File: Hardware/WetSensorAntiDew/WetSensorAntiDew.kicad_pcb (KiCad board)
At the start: 2 copper layers, 38.1 x 48.8 mm, 30 parts, among them J2 Connector to BME280, J3 4P4C, J5 Connector to power supply, J6 Conn_01x04_Socket, J8 6P6C, Q1 MOSFET N-CH, SW1 SW_Push, U1 AMS1117, U3 STM32F103C6Tx, Y1 Crystal_GND24_Small

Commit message: added USNA logo
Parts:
- added ?: LOGO, footprints:Anchors Aweigh, B.Cu at (112.1, 112.6)
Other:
- outline, holes or cut-outs redrawn

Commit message: shrunk anchors aweigh
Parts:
- moved ? 21.9 mm to (129.0, 98.7)

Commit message: USNA emblem tweaks
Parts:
- moved ? 23.1 mm to (107.2, 106.2)
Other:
- board text added: "Go Navy Beat Army"

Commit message: Added Semper Supra :)
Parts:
- added G***: LOGO, footprints:Semper Supra, B.Cu at (125.1, 109.3)

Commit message: Finalized silkscreen
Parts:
- added G***: LOGO, footprints:Evergreen, B.Cu at (98.1, 93.4)
- moved G*** 0.18 mm to (124.9, 109.3)
- renumbered SW1 to RESET
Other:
- board text added: "Go Navy, Beat Army"
- board text added: "V D C G"
- board text removed: "Go Navy Beat Army"

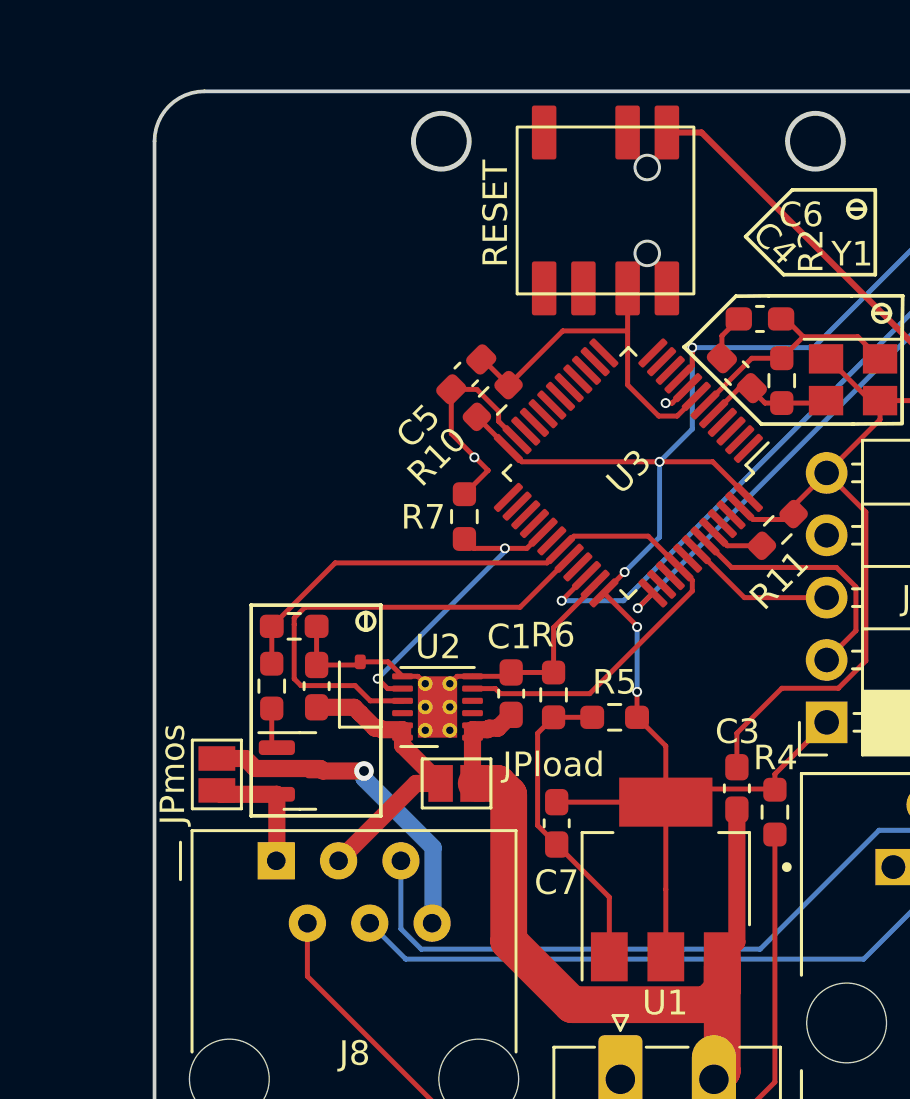
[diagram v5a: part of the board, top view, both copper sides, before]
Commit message: Tuned pinouts, corrected N/P switches
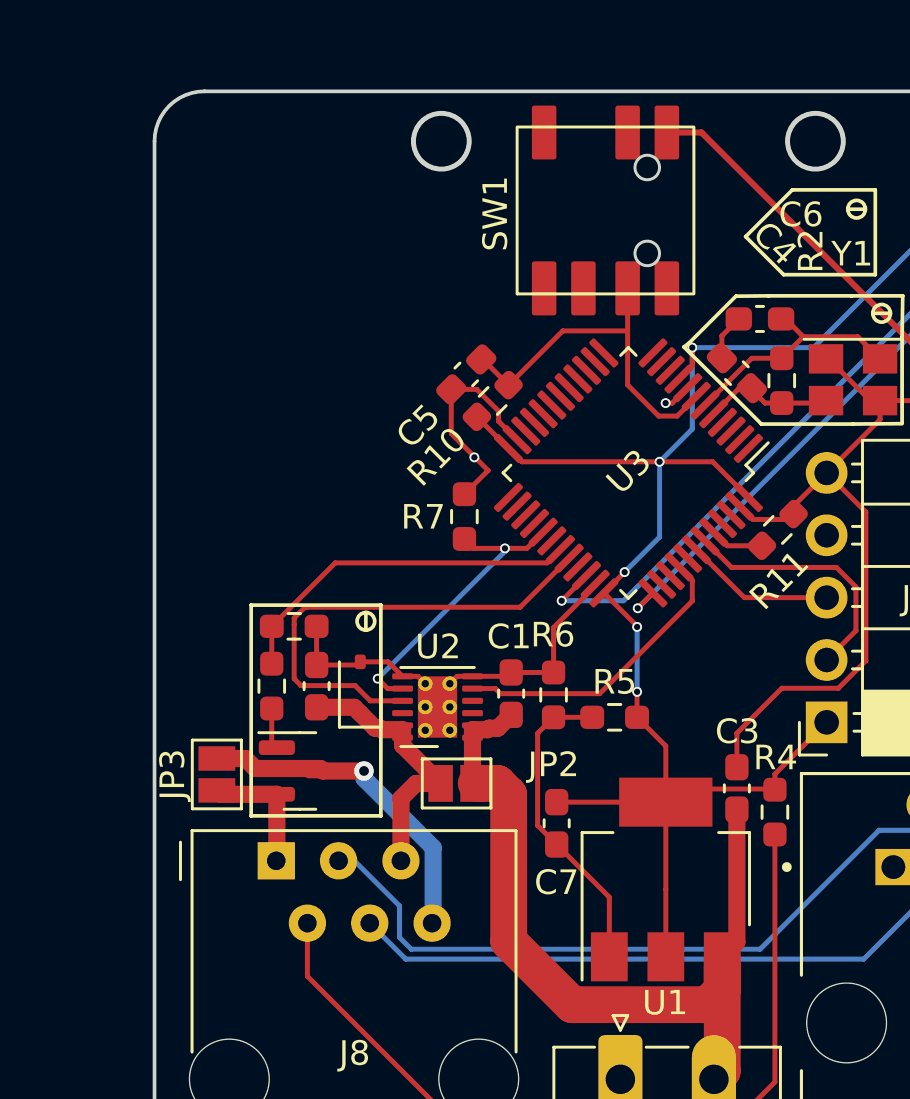
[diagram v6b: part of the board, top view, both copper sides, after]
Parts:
- renumbered JPload to JP2, JPmos to JP3, RESET to SW1
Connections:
- J8 pad 3: +12C -> WET1
- J8 pad 5: WET1 -> +12C
- R1 pad 2: PIN6 -> NFET
- R3 pad 2: PIN6 -> NFET
- U2 pad 5: PIN6 -> PFET
- U3 pad 31: PIN6 -> NFET
- U3 pad 40: PIN6 -> PFET
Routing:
- net PIN6: track 32.1 -> 0.00 mm
- net NFET: track 0.00 -> 14.6 mm
- net PFET: track 0.00 -> 12.2 mm
- net WET1: track 29.4 -> 31.1 mm
- net +12C: track 12.2 -> 11.1 mm

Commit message: Reset silk, corrected prog header
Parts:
- renumbered SW1 to SWRESET
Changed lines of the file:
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@@
     (property "ki_keywords" "switch normally-open pushbutton push-button")
     (attr smd)
-    (fp_text reference "SW1" (at 0.127 4.478631 90 unlocked) (layer "F.SilkS")
+    (fp_text reference "SWRESET" (at 0.127 4.478631 90 unlocked) (layer "F.SilkS")
         (effects (font (size 1 1) (thickness 0.15)))
     )
@@
     (fp_line (start -1.35 3.4) (end -1.35 -2.6)
       (stroke (width 0.12) (type solid)) (layer "F.SilkS"))
-    (fp_line (start 0 2.29) (end 5.08 2.29)
-      (stroke (width 0.12) (type solid)) (layer "F.SilkS"))
-    (fp_line (start 0 3.3) (end 0 2.29)
-      (stroke (width 0.12) (type solid)) (layer "F.SilkS"))
-    (fp_line (start 5.08 2.29) (end 5.08 3.3)
-      (stroke (width 0.12) (type solid)) (layer "F.SilkS"))
     (fp_line (start 5.75 -2.55) (end 8.95 -2.55)
       (stroke (width 0.12) (type solid)) (layer "F.SilkS"))
@@
     (fp_line (start -1.2 3.3) (end -1.25 3.3)
       (stroke (width 0.1) (type solid)) (layer "F.Fab"))
-    (fp_line (start 0 2.3) (end 0 3.3)
-      (stroke (width 0.1) (type solid)) (layer "F.Fab"))
-    (fp_line (start 5.1 2.3) (end 0 2.3)
-      (stroke (width 0.1) (type solid)) (layer "F.Fab"))
-    (fp_line (start 5.1 3.3) (end 5.1 2.3)
-      (stroke (width 0.1) (type solid)) (layer "F.Fab"))
     (fp_line (start 5.75 -2.5) (end 8.85 -2.5)

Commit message: Final design review pre-fab tuning
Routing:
- net +3V3: track 68.9 -> 72.6 mm
- net Earth: track 80.6 -> 79.9 mm
